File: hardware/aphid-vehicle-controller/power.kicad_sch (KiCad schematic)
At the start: 39 parts, among them U2 LD1117S33TR_SOT223, U3 LMR33630BDDA

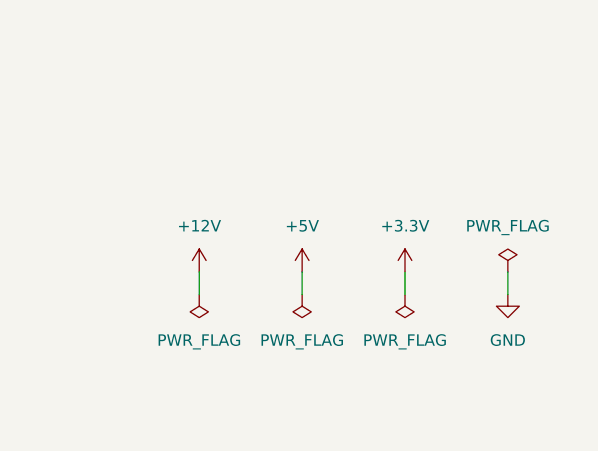
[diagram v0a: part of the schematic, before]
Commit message: ERC check passing
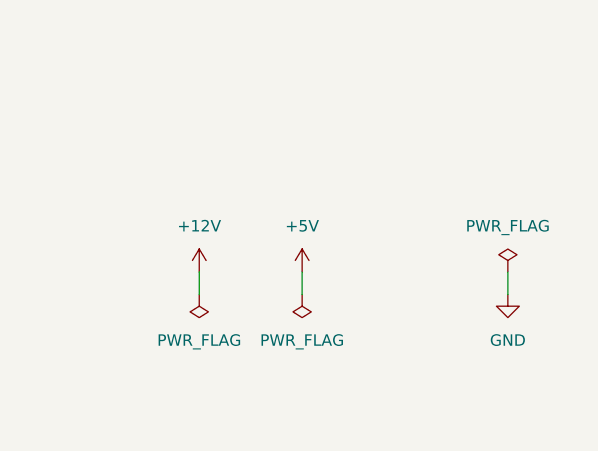
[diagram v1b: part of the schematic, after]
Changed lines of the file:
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@@
 	(wire
 		(pts
-			(xy 265.43 153.67) (xy 265.43 156.21)
-		)
-		(stroke
-			(width 0)
-			(type default)
-		)
-	)
-	(wire
-		(pts
 			(xy 255.27 36.83) (xy 255.27 39.37)
 		)
@@
 	)
 	(symbol
-		(lib_id "power:+3.3V")
-		(at 265.43 153.67 0)
-		(unit 1)
-		(exclude_from_sim no)
-		(in_bom yes)
-		(on_board yes)
-		(dnp no)
-		(fields_autoplaced yes)
-		(property "Reference" "#PWR063"
-			(at 265.43 157.48 0)
-			(effects
-				(font
-					(size 1.27 1.27)
-				)
-				(hide yes)
-			)
-		)
-		(property "Value" "+3.3V"
-			(at 265.43 148.59 0)
-			(effects
-				(font
-					(size 1.27 1.27)
-				)
-			)
-		)
-		(property "Footprint" ""
-			(at 265.43 153.67 0)
-			(effects
-				(font
-					(size 1.27 1.27)
-				)
-				(hide yes)
-			)
-		)
-		(property "Datasheet" ""
-			(at 265.43 153.67 0)
-			(effects
-				(font
-					(size 1.27 1.27)
-				)
-				(hide yes)
-			)
-		)
-		(property "Description" "Power symbol creates a global label with name \"+3.3V\""
-			(at 265.43 153.67 0)
-			(effects
-				(font
-					(size 1.27 1.27)
-				)
-				(hide yes)
-			)
-		)
-		(pin "1"
-		)
-		(instances
-			(project "aphid-vehicle-controller"
-				(path "/1bdad060-e59b-443f-afdb-9aa678a43546/98781d90-1f08-466f-be3c-fdb64160be3c"
-					(reference "#PWR063")
-					(unit 1)
-				)
-			)
-		)
-	)
-	(symbol
 		(lib_id "Device:C")
 		(at 77.47 40.64 0)
@@
 					(unit 1)
 				)
-			)
-		)
-	)
-	(symbol
-		(lib_id "power:PWR_FLAG")
-		(at 265.43 156.21 180)
-		(unit 1)
-		(exclude_from_sim no)
-		(in_bom yes)
-		(on_board yes)
-		(dnp no)
-		(fields_autoplaced yes)
-		(property "Reference" "#FLG04"
-			(at 265.43 158.115 0)
-			(effects
-				(font
-					(size 1.27 1.27)
-				)
-				(hide yes)
-			)
-		)
-		(property "Value" "PWR_FLAG"
-			(at 265.43 161.29 0)
-			(effects
-				(font
-					(size 1.27 1.27)
-				)
-			)
-		)
-		(property "Footprint" ""
-			(at 265.43 156.21 0)
-			(effects
-				(font
-					(size 1.27 1.27)
-				)
-				(hide yes)
-			)
-		)
-		(property "Datasheet" "~"
-			(at 265.43 156.21 0)
-			(effects
-				(font
-					(size 1.27 1.27)
-				)
-				(hide yes)
-			)
-		)
-		(property "Description" "Special symbol for telling ERC where power comes from"
-			(at 265.43 156.21 0)
-			(effects
-				(font
-					(size 1.27 1.27)
-				)
-				(hide yes)
-			)
-		)
-		(pin "1"
-		)
-		(instances
-			(project "aphid-vehicle-controller"
-				(path "/1bdad060-e59b-443f-afdb-9aa678a43546/98781d90-1f08-466f-be3c-fdb64160be3c"
-					(reference "#FLG04")
-					(unit 1)
-				)
